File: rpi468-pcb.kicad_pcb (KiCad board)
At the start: 2 copper layers, 11 parts, among them J1 USB_A, J2 USB_C_Receptacle_USB2.0, J3 Conn_01x04_Female, U1 LM397

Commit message: moved some components
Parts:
- moved R6 7.25 mm to (149.1, 78.4), turned to 180 degrees
- moved R5 2.96 mm to (145.4, 76.1), turned to 0 degrees
- moved J3 1.90 mm to (158.6, 82.1)
- moved S1 1.20 mm to (153.7, 80.9)
- moved R4 0.51 mm to (145.4, 82.7)
- moved R3 0.42 mm to (148.3, 81.9)
- moved R1 0.39 mm to (154.7, 73.4)
- moved R2 0.38 mm to (151.1, 73.4)
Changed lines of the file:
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@@
   (net 14 "Net-(R5-Pad2)")
   (footprint "Resistor_SMD:R_0805_2012Metric" (layer "F.Cu")
-    (at 141.8825 79.0975 90)
+    (at 149.098 78.359 180)
     (descr "Resistor SMD 0805 (2012 Metric), square (rectangular) end terminal, IPC_7351 nominal, (Body size source: IPC-SM-782 page 72, https://www.pcb-3d.com/wordpress/wp-content/uploads/ipc-sm-782a_amendment_1_and_2.pdf), generated with kicad-footprint-generator")
     (tags "resistor")
@@
     (property "Sheetname" "")
     (attr smd)
-    (fp_text reference "R6" (at 0 -1.65 90) (layer "F.SilkS")
-      (effects (font (size 1 1) (thickness 0.15)))
-    )
-    (fp_text value "5.1k" (at 0 1.65 90) (layer "F.Fab")
-      (effects (font (size 1 1) (thickness 0.15)))
-    )
-    (fp_text user "${REFERENCE}" (at 0 0 90) (layer "F.Fab")
+    (fp_text reference "R6" (at 0 -1.65) (layer "F.SilkS")
+      (effects (font (size 1 1) (thickness 0.15)))
+    )
+    (fp_text value "5.1k" (at 0 1.65) (layer "F.Fab")
+      (effects (font (size 1 1) (thickness 0.15)))
+    )
+    (fp_text user "${REFERENCE}" (at 0 0) (layer "F.Fab")
       (effects (font (size 0.5 0.5) (thickness 0.08)))
     )
@@
     (fp_line (start -1 -0.625) (end 1 -0.625) (layer "F.Fab") (width 0.1))
     (fp_line (start 1 0.625) (end -1 0.625) (layer "F.Fab") (width 0.1))
-    (pad "1" smd roundrect (at -0.9125 0 90) (size 1.025 1.4) (layers "F.Cu" "F.Paste" "F.Mask") (roundrect_rratio 0.243902)
+    (pad "1" smd roundrect (at -0.9125 0 180) (size 1.025 1.4) (layers "F.Cu" "F.Paste" "F.Mask") (roundrect_rratio 0.243902)
       (net 1 "+5V") (pintype "passive"))
-    (pad "2" smd roundrect (at 0.9125 0 90) (size 1.025 1.4) (layers "F.Cu" "F.Paste" "F.Mask") (roundrect_rratio 0.243902)
+    (pad "2" smd roundrect (at 0.9125 0 180) (size 1.025 1.4) (layers "F.Cu" "F.Paste" "F.Mask") (roundrect_rratio 0.243902)
       (net 14 "Net-(R5-Pad2)") (pintype "passive"))
     (model "${KICAD6_3DMODEL_DIR}/Resistor_SMD.3dshapes/R_0805_2012Metric.wrl"
@@
   )
   (footprint "Resistor_SMD:R_0805_2012Metric" (layer "F.Cu")
-    (at 142.5175 75.565 180)
+    (at 145.4385 76.073)
     (descr "Resistor SMD 0805 (2012 Metric), square (rectangular) end terminal, IPC_7351 nominal, (Body size source: IPC-SM-782 page 72, https://www.pcb-3d.com/wordpress/wp-content/uploads/ipc-sm-782a_amendment_1_and_2.pdf), generated with kicad-footprint-generator")
     (tags "resistor")
@@
     (fp_line (start -1 -0.625) (end 1 -0.625) (layer "F.Fab") (width 0.1))
     (fp_line (start 1 -0.625) (end 1 0.625) (layer "F.Fab") (width 0.1))
-    (pad "1" smd roundrect (at -0.9125 0 180) (size 1.025 1.4) (layers "F.Cu" "F.Paste" "F.Mask") (roundrect_rratio 0.243902)
+    (pad "1" smd roundrect (at -0.9125 0) (size 1.025 1.4) (layers "F.Cu" "F.Paste" "F.Mask") (roundrect_rratio 0.243902)
       (net 13 "Net-(R3-Pad2)") (pintype "passive"))
-    (pad "2" smd roundrect (at 0.9125 0 180) (size 1.025 1.4) (layers "F.Cu" "F.Paste" "F.Mask") (roundrect_rratio 0.243902)
+    (pad "2" smd roundrect (at 0.9125 0) (size 1.025 1.4) (layers "F.Cu" "F.Paste" "F.Mask") (roundrect_rratio 0.243902)
       (net 14 "Net-(R5-Pad2)") (pintype "passive"))
     (model "${KICAD6_3DMODEL_DIR}/Resistor_SMD.3dshapes/R_0805_2012Metric.wrl"
@@
   )
   (footprint "Resistor_SMD:R_0805_2012Metric" (layer "F.Cu")
-    (at 145.415 83.185 180)
+    (at 145.4385 82.677 180)
     (descr "Resistor SMD 0805 (2012 Metric), square (rectangular) end terminal, IPC_7351 nominal, (Body size source: IPC-SM-782 page 72, https://www.pcb-3d.com/wordpress/wp-content/uploads/ipc-sm-782a_amendment_1_and_2.pdf), generated with kicad-footprint-generator")
     (tags "resistor")
@@
   )
   (footprint "Resistor_SMD:R_0805_2012Metric" (layer "F.Cu")
-    (at 151.13 73.025)
+    (at 151.1065 73.406)
     (descr "Resistor SMD 0805 (2012 Metric), square (rectangular) end terminal, IPC_7351 nominal, (Body size source: IPC-SM-782 page 72, https://www.pcb-3d.com/wordpress/wp-content/uploads/ipc-sm-782a_amendment_1_and_2.pdf), generated with kicad-footprint-generator")
     (tags "resistor")
@@
   )
   (footprint "Connector_Wuerth:Wuerth_WR-WTB_64800411622_1x04_P1.50mm_Vertical" (layer "F.Cu")
-    (at 160.02 83.415 90)
+    (at 158.623 82.121 90)
     (descr "Wuerth WR-WTB series connector, 64800411622 (https://katalog.we-online.com/em/datasheet/6480xx11622.pdf), generated with kicad-footprint-generator")
     (tags "connector Wuerth WR-WTB vertical")
@@
   )
   (footprint "Resistor_SMD:R_0805_2012Metric" (layer "F.Cu")
-    (at 154.5825 73.025 180)
+    (at 154.686 73.406 180)
     (descr "Resistor SMD 0805 (2012 Metric), square (rectangular) end terminal, IPC_7351 nominal, (Body size source: IPC-SM-782 page 72, https://www.pcb-3d.com/wordpress/wp-content/uploads/ipc-sm-782a_amendment_1_and_2.pdf), generated with kicad-footprint-generator")
     (tags "resistor")
@@
   )
   (footprint "Package_DFN_QFN:TDFN-10-1EP_2x3mm_P0.5mm_EP0.9x2mm_ThermalVias" (layer "F.Cu")
-    (at 154.305 81.915)
+    (at 153.67 80.899)
     (descr "TDFN, 10 Pin (https://pdfserv.maximintegrated.com/package_dwgs/21-0429.PDF), generated with kicad-footprint-generator ipc_noLead_generator.py")
     (tags "TDFN NoLead")
@@
   )
   (footprint "Resistor_SMD:R_0805_2012Metric" (layer "F.Cu")
-    (at 148.59 82.2725 -90)
+    (at 148.336 81.9385 -90)
     (descr "Resistor SMD 0805 (2012 Metric), square (rectangular) end terminal, IPC_7351 nominal, (Body size source: IPC-SM-782 page 72, https://www.pcb-3d.com/wordpress/wp-content/uploads/ipc-sm-782a_amendment_1_and_2.pdf), generated with kicad-footprint-generator")
     (tags "resistor")

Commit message: trying to route
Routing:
- net GND: track 0.00 -> 46.9 mm, vias 0 -> 3
- net +5V: track 0.00 -> 39.0 mm, vias 0 -> 3
- net Net-(J2-PadA7): track 0.00 -> 25.8 mm, vias 0 -> 1
- net Net-(J2-PadA5): track 0.00 -> 23.4 mm, vias 0 -> 2
- net Net-(J3-Pad3): track 0.00 -> 15.1 mm, vias 0 -> 2
- net Net-(J2-PadB5): track 0.00 -> 13.0 mm, vias 0 -> 1
- net Net-(R5-Pad2): track 0.00 -> 11.0 mm
- net Net-(J1-Pad2): track 0.00 -> 8.22 mm
- net Net-(J2-PadA6): track 0.00 -> 8.05 mm
- net Net-(J1-Pad3): track 0.00 -> 6.44 mm, vias 0 -> 2
- net Net-(J3-Pad2): track 0.00 -> 4.47 mm
- net Net-(R3-Pad2): track 0.00 -> 4.23 mm
- added copper zone on B.Cu, net +5V
- added copper zone on F.Cu, net GND
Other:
- board outline added: 17.8 x 21.6 mm

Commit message: layingout the board again
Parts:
- J2: footprint Connector_USB:USB_C_Receptacle_Amphenol_12401548E4-2A -> Connector_USB:USB_C_Receptacle_Amphenol_12401610E4-2A
- R1, R2, R3, R4, R5, R6: footprint Resistor_SMD:R_0805_2012Metric -> Resistor_SMD:R_0603_1608Metric_Pad0.98x0.95mm_HandSolder
- S1: footprint Package_DFN_QFN:TDFN-10-1EP_2x3mm_P0.5mm_EP0.9x2mm_ThermalVias -> Package_DFN_QFN:DFN-10-1EP_3x3mm_P0.5mm_EP1.75x2.7mm
- moved R5 40.0 mm to (165.3, 110.7)
- moved R6 37.8 mm to (168.6, 110.7)
- moved J3 36.8 mm to (164.9, 118.4), turned to 0 degrees
- moved S1 35.4 mm to (176.3, 108.2), turned to 90 degrees
- moved U1 34.9 mm to (166.2, 107.4)
- moved R4 34.5 mm to (169.7, 107.2), turned to 0 degrees
- moved R3 34.2 mm to (169.7, 108.7), turned to 180 degrees
- moved J2 33.9 mm to (170.9, 94.5)
- moved J1 32.5 mm to (174.4, 102.5)
- moved R1 30.7 mm to (177.0, 94.5), turned to 90 degrees
- moved R2 25.1 mm to (164.6, 94.6), turned to 90 degrees
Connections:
- S1 pad 2: Net-(J1-Pad3) -> Net-(J1-Pad2)
- S1 pad 3: Net-(J2-PadA6) -> Net-(J1-Pad3)
- S1 pad 8: Net-(J1-Pad2) -> Net-(J2-PadA6)
- U1 pad 1: Net-(J2-PadA5) -> Net-(J2-PadB5)
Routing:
- net GND: track 46.9 -> 0.00 mm, vias 3 -> 0
- net +5V: track 39.0 -> 0.00 mm, vias 3 -> 0
- net Net-(J2-PadA7): track 25.8 -> 0.00 mm, vias 1 -> 0
- net Net-(J2-PadA5): track 23.4 -> 0.00 mm, vias 2 -> 0
- net Net-(J3-Pad3): track 15.1 -> 0.00 mm, vias 2 -> 0
- net Net-(J2-PadB5): track 13.0 -> 0.00 mm, vias 1 -> 0
- net Net-(R5-Pad2): track 11.0 -> 0.00 mm
- net Net-(J1-Pad2): track 8.22 -> 0.00 mm
- net Net-(J2-PadA6): track 8.05 -> 0.00 mm
- net Net-(J1-Pad3): track 6.44 -> 0.00 mm, vias 2 -> 0
- net Net-(J3-Pad2): track 4.47 -> 0.00 mm
- net Net-(R3-Pad2): track 4.23 -> 0.00 mm
- removed copper zone on B.Cu, net +5V
- removed copper zone on F.Cu, net GND
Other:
- board outline removed

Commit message: updated layout a little
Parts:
- moved J3 6.41 mm to (170.1, 114.7), turned to 180 degrees
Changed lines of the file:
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@@
   (net 14 "Net-(R5-Pad2)")
   (footprint "Connector_Wuerth:Wuerth_WR-WTB_64800411622_1x04_P1.50mm_Vertical" (layer "F.Cu")
-    (at 164.882 118.364)
+    (at 170.132 114.681 180)
     (descr "Wuerth WR-WTB series connector, 64800411622 (https://katalog.we-online.com/em/datasheet/6480xx11622.pdf), generated with kicad-footprint-generator")
     (tags "connector Wuerth WR-WTB vertical")
@@
     (fp_line (start 6 -1.3) (end -1.5 -1.3) (layer "F.Fab") (width 0.1))
     (fp_line (start -1.5 -1.3) (end -1.5 2.2) (layer "F.Fab") (width 0.1))
-    (pad "1" thru_hole roundrect (at 0 0) (size 1.17 1.87) (drill 0.87) (layers *.Cu *.Mask) (roundrect_rratio 0.213675)
+    (pad "1" thru_hole roundrect (at 0 0 180) (size 1.17 1.87) (drill 0.87) (layers *.Cu *.Mask) (roundrect_rratio 0.213675)
       (net 1 "+5V") (pinfunction "Pin_1") (pintype "passive"))
-    (pad "2" thru_hole oval (at 1.5 0) (size 1.17 1.87) (drill 0.87) (layers *.Cu *.Mask)
+    (pad "2" thru_hole oval (at 1.5 0 180) (size 1.17 1.87) (drill 0.87) (layers *.Cu *.Mask)
       (net 11 "Net-(J3-Pad2)") (pinfunction "Pin_2") (pintype "passive"))
-    (pad "3" thru_hole oval (at 3 0) (size 1.17 1.87) (drill 0.87) (layers *.Cu *.Mask)
+    (pad "3" thru_hole oval (at 3 0 180) (size 1.17 1.87) (drill 0.87) (layers *.Cu *.Mask)
       (net 12 "Net-(J3-Pad3)") (pinfunction "Pin_3") (pintype "passive"))
-    (pad "4" thru_hole oval (at 4.5 0) (size 1.17 1.87) (drill 0.87) (layers *.Cu *.Mask)
+    (pad "4" thru_hole oval (at 4.5 0 180) (size 1.17 1.87) (drill 0.87) (layers *.Cu *.Mask)
       (net 4 "GND") (pinfunction "Pin_4") (pintype "passive"))
     (model "${KICAD6_3DMODEL_DIR}/Connector_Wuerth.3dshapes/Wuerth_WR-WTB_64800411622_1x04_P1.50mm_Vertical.wrl"

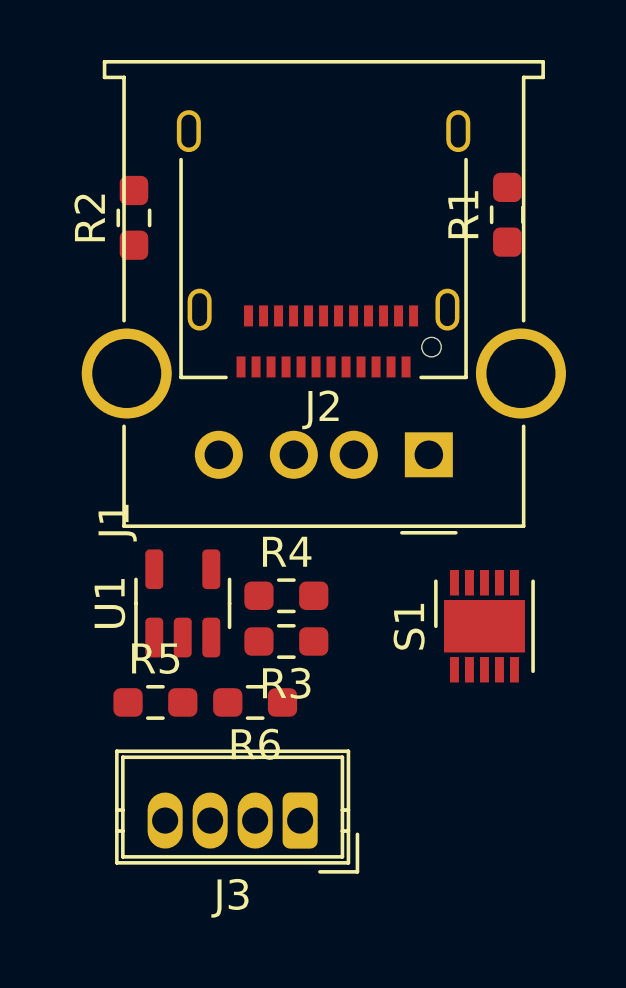
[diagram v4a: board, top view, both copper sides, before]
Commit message: made some tracks
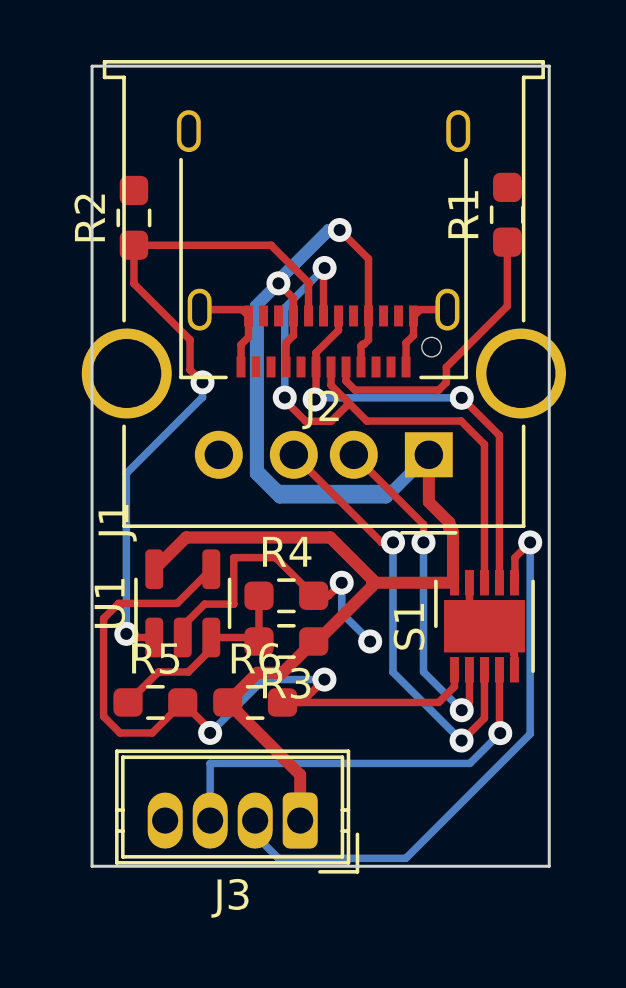
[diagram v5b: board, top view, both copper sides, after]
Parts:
- turned R6 to 0 degrees
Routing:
- net +5V: track 0.00 -> 81.0 mm, vias 0 -> 2
- net Net-(R5-Pad2): track 0.00 -> 25.0 mm, vias 0 -> 2
- net Net-(J2-PadB5): track 0.00 -> 23.4 mm, vias 0 -> 2
- net Net-(J2-PadA6): track 0.00 -> 20.4 mm, vias 0 -> 2
- net Net-(J3-Pad2): track 0.00 -> 19.6 mm, vias 0 -> 1
- net GND: track 0.00 -> 19.3 mm, vias 0 -> 2
- net Net-(J1-Pad3): track 0.00 -> 14.8 mm, vias 0 -> 2
- net Net-(J2-PadA7): track 0.00 -> 14.7 mm, vias 0 -> 2
- net Net-(J3-Pad3): track 0.00 -> 14.1 mm, vias 0 -> 1
- net Net-(J1-Pad2): track 0.00 -> 11.5 mm, vias 0 -> 2
- net Net-(J2-PadA5): track 0.00 -> 9.56 mm
- net Net-(R3-Pad2): track 0.00 -> 7.07 mm
- added copper zone on B.Cu, net GND
- added copper zone on F.Cu, net GND
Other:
- board outline added: 15.2 x 26.7 mm

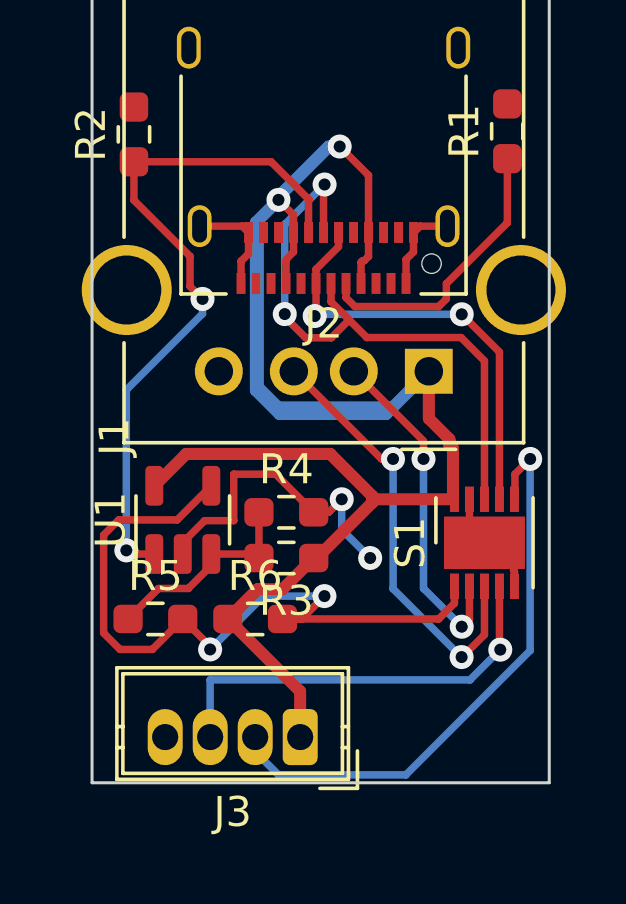
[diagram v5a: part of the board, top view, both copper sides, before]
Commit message: routing seems more reasonable, still need to refer to mCAD for actual cut profile
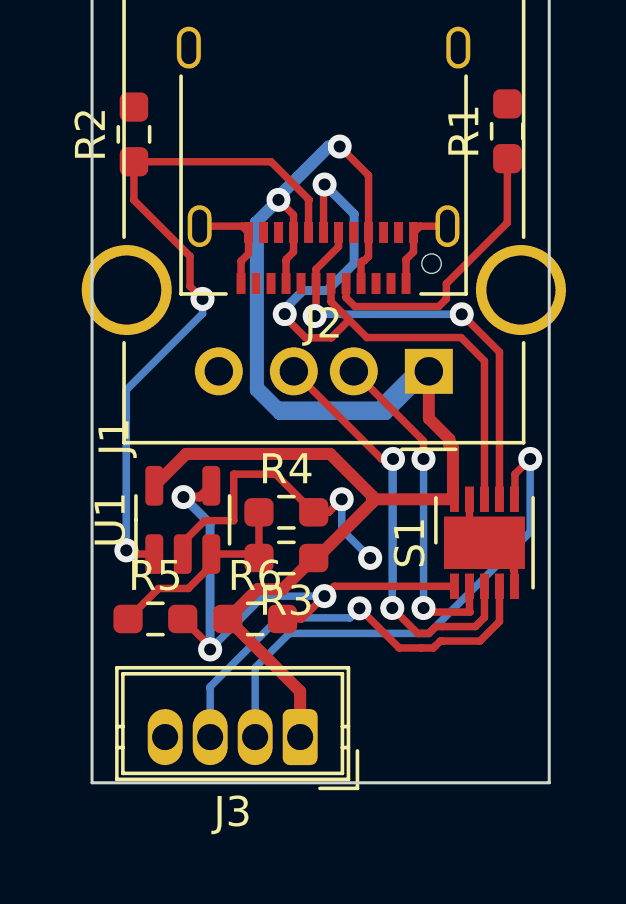
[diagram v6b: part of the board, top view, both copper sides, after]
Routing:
- net Net-(R5-Pad2): track 25.0 -> 18.7 mm, vias 2 -> 3
- net Net-(J1-Pad3): track 14.8 -> 18.5 mm
- net Net-(J3-Pad2): track 19.6 -> 17.8 mm
- net Net-(J2-PadA6): track 20.4 -> 21.7 mm
